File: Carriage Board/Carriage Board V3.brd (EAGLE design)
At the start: 82.6 x 49.6 mm, 22 parts, among them J1 C, J2 NC, J3 NO, J4 TERMINALBLOCK/4PIN/5MMPITCH, K1 68612014122, X1 EXTRUDER MOTOR, X2 AOF, X3 CF, X4 CF

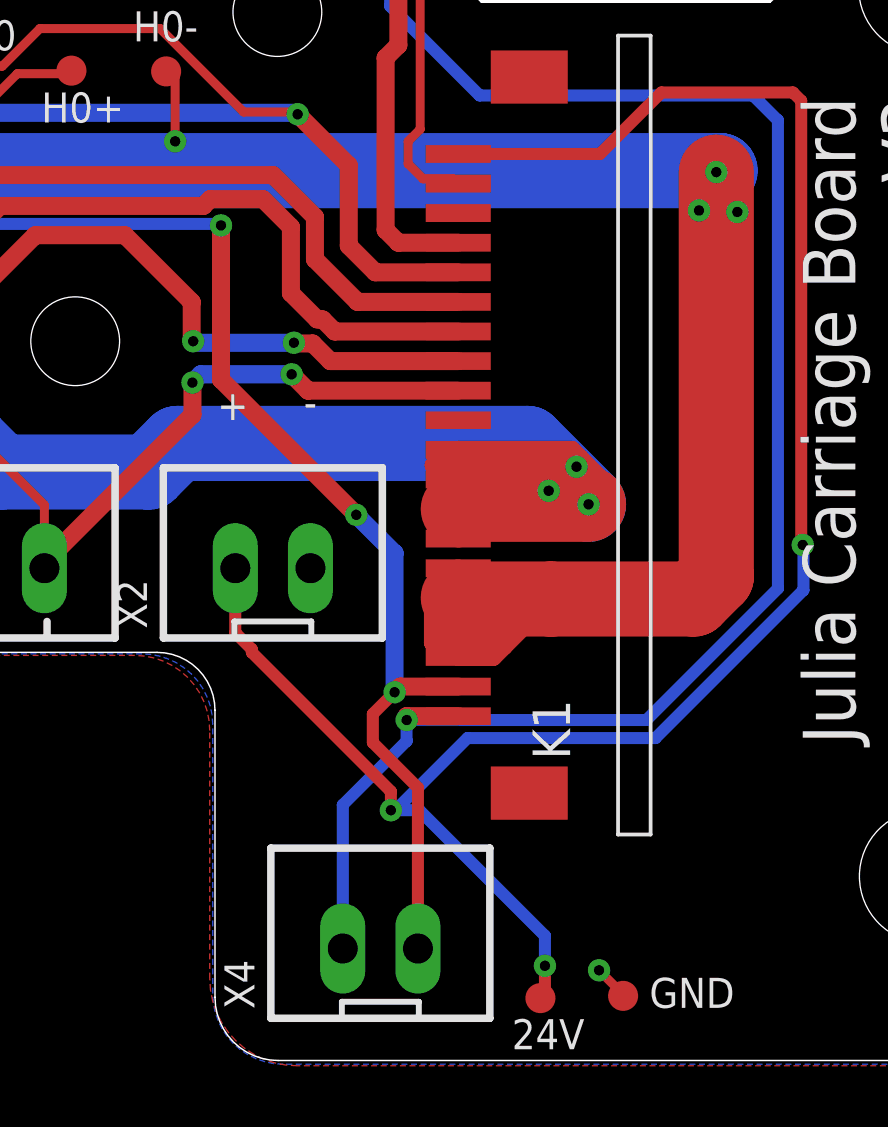
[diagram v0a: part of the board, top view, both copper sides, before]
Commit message: Missing link in the GND wire routing rectified
The missing link in the GND wire has been rectified and routed consecutively in the Carriage board V3 of the Julia electronics file
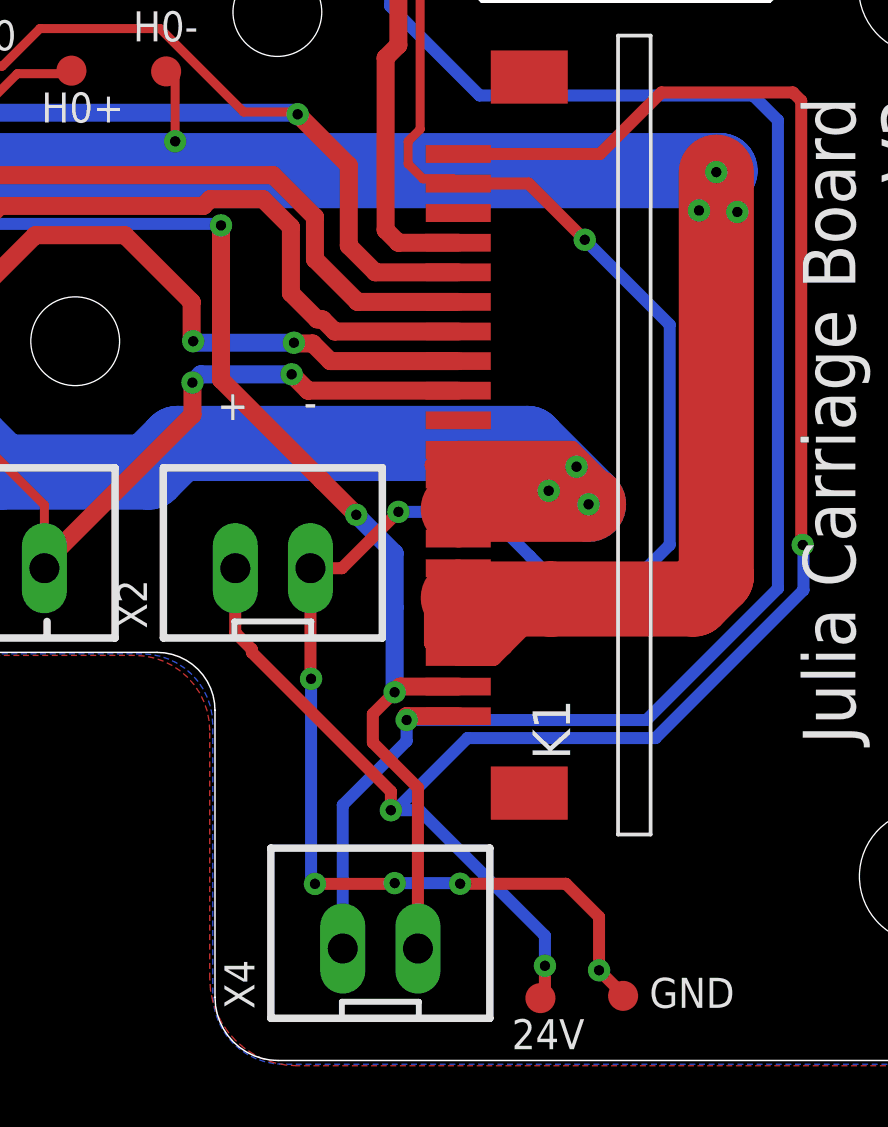
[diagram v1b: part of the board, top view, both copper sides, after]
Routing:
- net GND: track 69.6 -> 123.7 mm, vias 2 -> 8
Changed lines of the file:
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@@
 <?xml version="1.0" encoding="utf-8"?>
 <!DOCTYPE eagle SYSTEM "eagle.dtd">
-<eagle version="9.5.2">
+<eagle version="9.6.2">
 <drawing>
 <settings>
@@
 <wire x1="14.224" y1="19.558" x2="13.9954" y2="19.431" width="0.3048" layer="1"/>
 <wire x1="20.32" y1="28.194" x2="20.4724" y2="28.194" width="0.3048" layer="1"/>
-<wire x1="67.9196" y1="-6.9342" x2="68.6816" y2="-7.6962" width="0.3048" layer="1"/>
+<wire x1="67.9196" y1="-6.9342" x2="68.6816" y2="-7.6962" width="0.4064" layer="1"/>
 <wire x1="68.6816" y1="-7.6962" x2="68.7324" y2="-7.7978" width="0.3048" layer="1"/>
 <wire x1="23.114" y1="28.194" x2="20.4724" y2="28.194" width="0.3048" layer="16"/>
@@
 <vertex x="2.4384" y="37.973" curve="-90"/>
 </polygon>
+<wire x1="58.166" y1="6.6548" x2="59.2328" y2="6.6548" width="0.4064" layer="1"/>
+<wire x1="59.2328" y1="6.6548" x2="61.1378" y2="8.5598" width="0.4064" layer="1"/>
+<via x="61.1378" y="8.5598" extent="1-16" drill="0.35"/>
+<wire x1="61.1378" y1="8.5598" x2="64.0842" y2="8.5598" width="0.4064" layer="16"/>
+<wire x1="64.0842" y1="8.5598" x2="65.5828" y2="7.0612" width="0.4064" layer="16"/>
+<wire x1="65.5828" y1="7.0612" x2="66.8274" y2="5.8166" width="0.4064" layer="16"/>
+<wire x1="66.8274" y1="5.8166" x2="68.6816" y2="5.8166" width="0.4064" layer="16"/>
+<wire x1="68.6816" y1="5.8166" x2="70.3072" y2="7.4422" width="0.4064" layer="16"/>
+<wire x1="70.3072" y1="7.4422" x2="70.3072" y2="14.8844" width="0.4064" layer="16"/>
+<wire x1="70.3072" y1="14.8844" x2="67.437" y2="17.7546" width="0.4064" layer="16"/>
+<via x="67.437" y="17.7546" extent="1-16" drill="0.35"/>
+<wire x1="67.437" y1="17.7546" x2="65.5372" y2="19.6544" width="0.4064" layer="1"/>
+<wire x1="65.5372" y1="19.6544" x2="63.162" y2="19.6544" width="0.4064" layer="1"/>
+<wire x1="58.166" y1="6.6548" x2="58.166" y2="2.93839375" width="0.4064" layer="1"/>
+<wire x1="58.166" y1="2.93839375" x2="58.187396875" y2="2.916996875" width="0.3048" layer="1"/>
+<via x="58.187396875" y="2.916996875" extent="1-16" drill="0.35"/>
+<wire x1="58.187396875" y1="2.916996875" x2="58.187396875" y2="-3.882196875" width="0.4064" layer="16"/>
+<wire x1="58.187396875" y1="-3.882196875" x2="58.3184" y2="-4.0132" width="0.3048" layer="16"/>
+<via x="58.3184" y="-4.0132" extent="1-16" drill="0.35"/>
+<wire x1="58.3184" y1="-4.0132" x2="61.087" y2="-4.0132" width="0.4064" layer="1"/>
+<wire x1="61.087" y1="-4.0132" x2="61.0616" y2="-3.9878" width="0.3048" layer="1"/>
+<wire x1="61.0616" y1="-3.9878" x2="61.0136" y2="-3.9878" width="0.3048" layer="1"/>
+<via x="61.0136" y="-3.9878" extent="1-16" drill="0.35"/>
+<wire x1="61.0136" y1="-3.9878" x2="63.20320625" y2="-3.9878" width="0.4064" layer="16"/>
+<wire x1="63.20320625" y1="-3.9878" x2="63.224603125" y2="-4.009196875" width="0.3048" layer="16"/>
+<via x="63.224603125" y="-4.009196875" extent="1-16" drill="0.35"/>
+<wire x1="63.224603125" y1="-4.009196875" x2="66.797996875" y2="-4.009196875" width="0.4064" layer="1"/>
+<wire x1="67.9196" y1="-5.1308" x2="67.9196" y2="-6.9342" width="0.4064" layer="1"/>
+<wire x1="66.797996875" y1="-4.009196875" x2="67.9196" y2="-5.1308" width="0.4064" layer="1"/>
 </signal>
 <signal name="CF-">
@@
 <wire x1="61.2014" y1="2.6544" x2="61.0108" y2="2.4638" width="0.6096" layer="1"/>
 <via x="61.0108" y="2.4638" extent="1-16" drill="0.35"/>
-<wire x1="61.0108" y1="2.4638" x2="61.0108" y2="7.1628" width="0.6096" layer="16"/>
+<wire x1="61.0108" y1="2.4638" x2="61.0108" y2="5.334" width="0.6096" layer="16"/>
+<wire x1="61.0108" y1="5.334" x2="61.0108" y2="7.1628" width="0.6096" layer="16"/>
 <wire x1="61.0108" y1="7.1628" x2="59.7154" y2="8.4582" width="0.6096" layer="16"/>
 <via x="59.7154" y="8.4582" extent="1-16" drill="0.35"/>
-<wire x1="59.7154" y1="8.4582" x2="55.1434" y2="13.0302" width="0.6096" layer="1"/>
+<wire x1="59.7154" y1="8.4582" x2="58.5597" y2="9.6139" width="0.6096" layer="1"/>
+<wire x1="58.5597" y1="9.6139" x2="55.1434" y2="13.0302" width="0.6096" layer="1"/>
 <wire x1="55.1434" y1="13.0302" x2="55.1434" y2="18.24" width="0.6096" layer="1"/>
 <via x="55.1434" y="18.24" extent="1-16" drill="0.35"/>
